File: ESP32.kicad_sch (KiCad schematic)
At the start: 5 parts

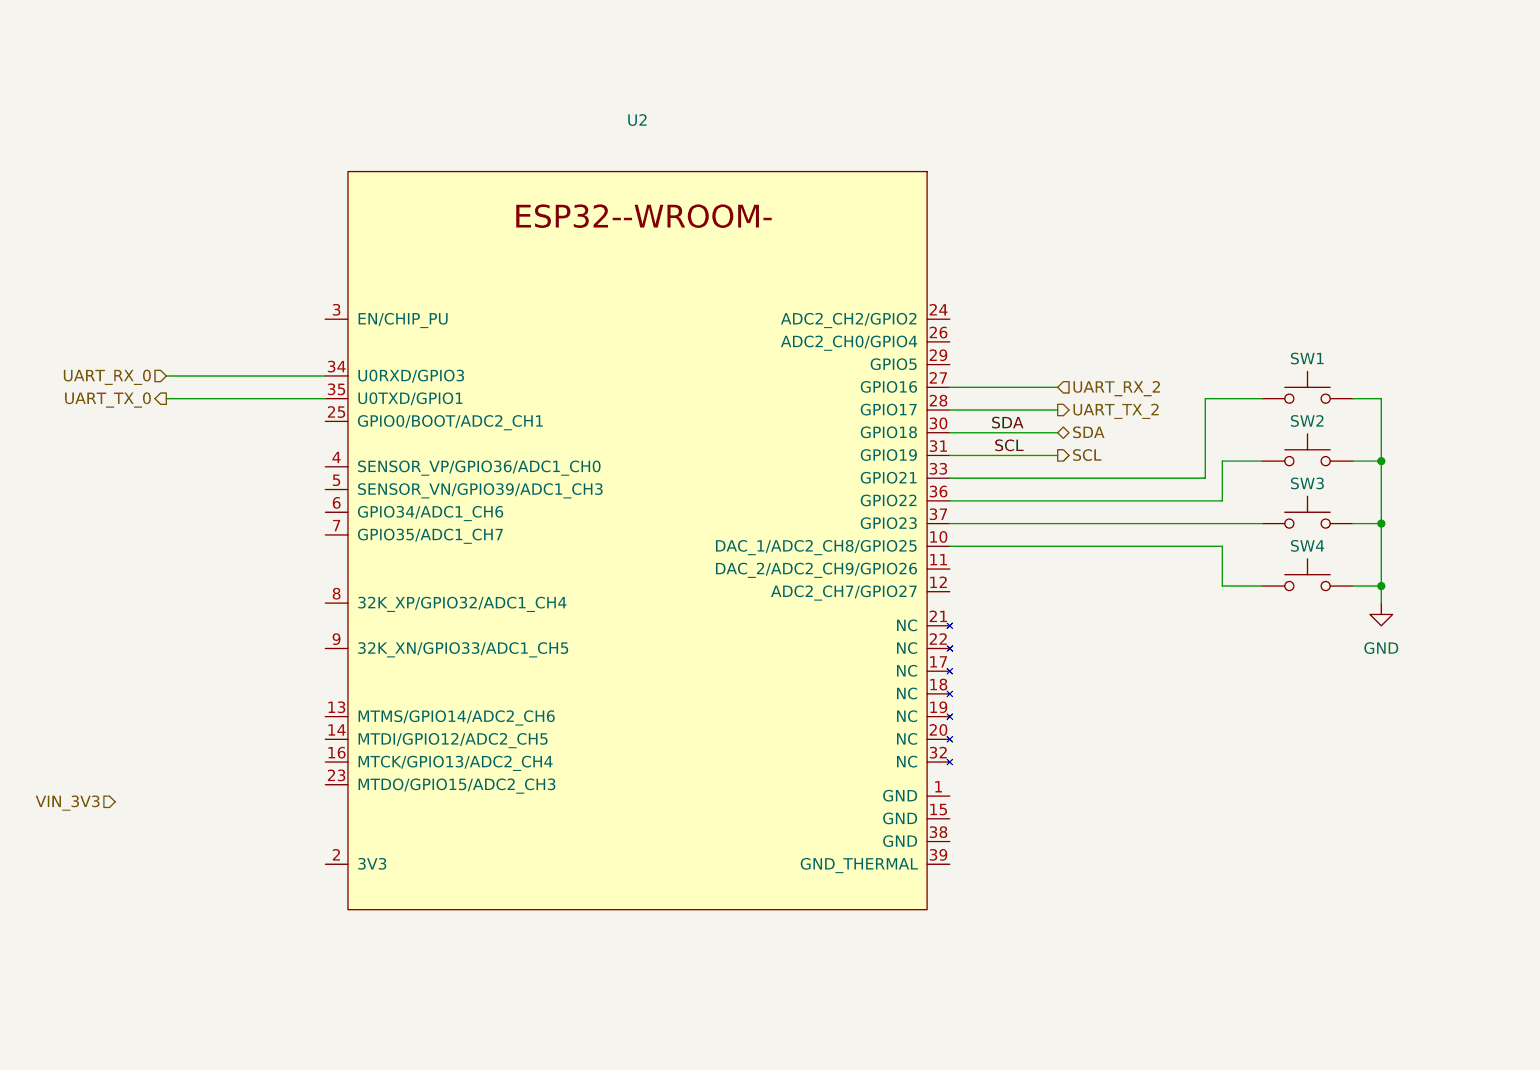
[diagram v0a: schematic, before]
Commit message: parcialmente terminada PCB falta verificar tamano de componentes
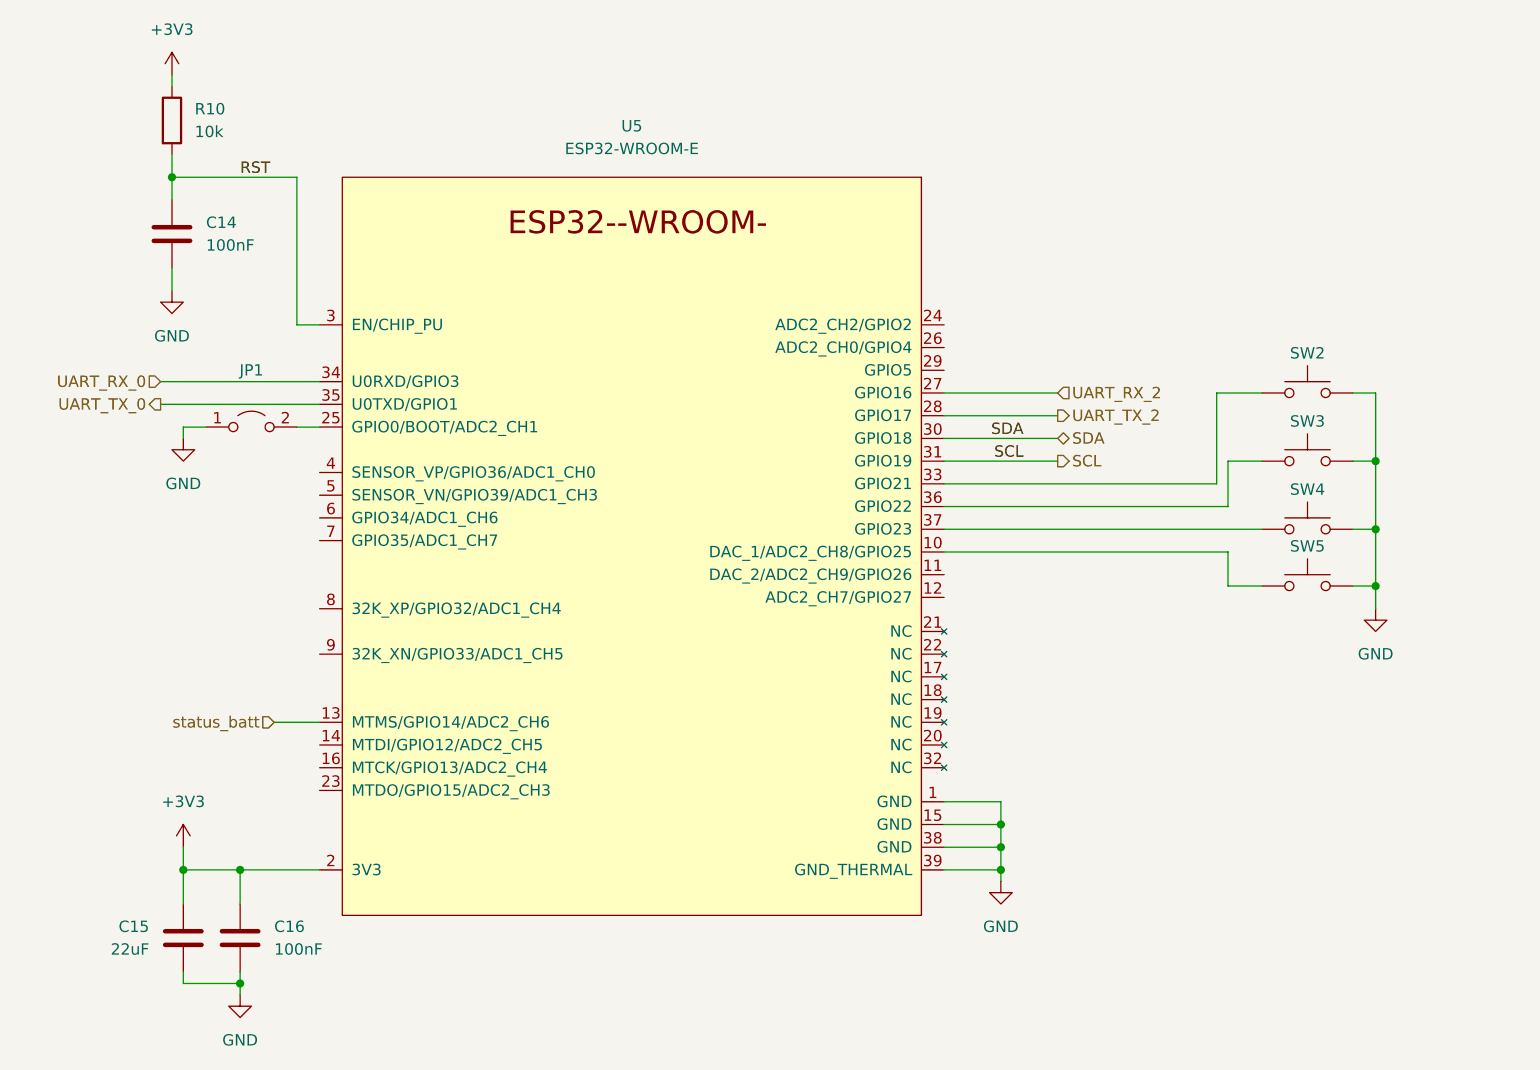
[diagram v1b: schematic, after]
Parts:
- added C14, C16: 100nF, Capacitor_SMD:C_0603_1608Metric_Pad1.08x0.95mm_HandSolder, symbol Device:C
- added C15: 22uF, Capacitor_SMD:C_0805_2012Metric_Pad1.18x1.45mm_HandSolder, symbol Device:C
- added JP1: (no value), symbol Jumper:Jumper_2_Open
- added R10: 10k, Resistor_SMD:R_0603_1608Metric_Pad0.98x0.95mm_HandSolder, symbol Device:R
- SW2: renamed from SW1; value (none) -> ~; footprint (none) -> Button_Switch_SMD:SW_SPST_PTS645
- SW3: renamed from SW2; value (none) -> ~; footprint (none) -> Button_Switch_SMD:SW_SPST_PTS645
- SW4: renamed from SW3; value (none) -> SW_Push; footprint (none) -> Button_Switch_SMD:SW_SPST_PTS645
- SW5: renamed from SW4; value (none) -> ~; footprint (none) -> Button_Switch_SMD:SW_SPST_PTS645
- U5: renamed from U2; value (none) -> ESP32-WROOM-E; footprint (none) -> Espressif:ESP32-WROOM-32E
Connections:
- net GND: now also U5.1 (GND), U5.15 (GND), U5.38 (GND), U5.39 (GND_THERMAL), C14.2, C15.2, C16.2, JP1.1 (A)
- net status_batt: now reaches U5.13 (MTMS/GPIO14/ADC2_CH6)
- net +3V3: now reaches U5.2 (3V3)
- net +3V3: now also C15.1, C16.1, R10.1
- net at U5.25 (GPIO0/BOOT/ADC2_CH1): now also JP1.2 (B)
- net RST: now reaches U5.3 (EN/CHIP_PU)
- net RST: now also C14.1, R10.2
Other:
- title: (none) -> GPS_CHECK
- moved on the sheet: SW2, SW4, U5

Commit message: terminando, aun falta una ultima revision previa a la fabricacion
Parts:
- JP1: value (none) -> Jumper_2_Open; footprint (none) -> Jumper:SolderJumper-2_P1.3mm_Open_RoundedPad1.0x1.5mm
- SW2, SW3, SW4, SW5: footprint Button_Switch_SMD:SW_SPST_PTS645 -> MSS_Devices:TL3301AF160QG
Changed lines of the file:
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@@
     (property "Reference" "SW5" (id 0) (at 222.25 98.425 0))
     (property "Value" "~" (id 1) (at 222.25 104.775 0))
-    (property "Footprint" "Button_Switch_SMD:SW_SPST_PTS645" (id 2) (at 222.25 97.79 0)
+    (property "Footprint" "MSS_Devices:TL3301AF160QG" (id 2) (at 222.25 97.79 0)
       (effects (font (size 1.27 1.27)) hide)
     )
@@
     (in_bom yes) (on_board yes) (fields_autoplaced)
     (property "Reference" "JP1" (id 0) (at 104.14 78.74 0))
-    (property "Value" "" (id 1) (at 104.14 81.28 0))
-    (property "Footprint" "" (id 2) (at 104.14 85.09 0)
+    (property "Value" "Jumper_2_Open" (id 1) (at 104.14 81.28 0))
+    (property "Footprint" "Jumper:SolderJumper-2_P1.3mm_Open_RoundedPad1.0x1.5mm" (id 2) (at 104.14 85.09 0)
       (effects (font (size 1.27 1.27)) hide)
     )
@@
     (property "Reference" "SW3" (id 0) (at 222.25 84.455 0))
     (property "Value" "~" (id 1) (at 222.25 83.185 0))
-    (property "Footprint" "Button_Switch_SMD:SW_SPST_PTS645" (id 2) (at 222.25 83.82 0)
+    (property "Footprint" "MSS_Devices:TL3301AF160QG" (id 2) (at 222.25 83.82 0)
       (effects (font (size 1.27 1.27)) hide)
     )
@@
       (effects (font (size 1.27 1.27)) hide)
     )
-    (property "Footprint" "Button_Switch_SMD:SW_SPST_PTS645" (id 2) (at 222.25 91.44 0)
+    (property "Footprint" "MSS_Devices:TL3301AF160QG" (id 2) (at 222.25 91.44 0)
       (effects (font (size 1.27 1.27)) hide)
     )
@@
     (property "Reference" "SW2" (id 0) (at 222.25 76.835 0))
     (property "Value" "~" (id 1) (at 222.25 75.565 0))
-    (property "Footprint" "Button_Switch_SMD:SW_SPST_PTS645" (id 2) (at 222.25 76.2 0)
+    (property "Footprint" "MSS_Devices:TL3301AF160QG" (id 2) (at 222.25 76.2 0)
       (effects (font (size 1.27 1.27)) hide)
     )

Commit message: generando gerbers
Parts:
- added R13, R14, R15, R16, R17, R18: 10k, Resistor_SMD:R_0603_1608Metric_Pad0.98x0.95mm_HandSolder, symbol Device:R
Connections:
- net +3V3: now also R15.1, R16.1, R17.1, R18.1
- net GND: now also R14.2
- net status_batt: now also R13.1; no longer U5.13 (MTMS/GPIO14/ADC2_CH6)
- net at SW5.1, U5.10 (DAC_1/ADC2_CH8/GPIO25): now also R18.2
- net at SW2.1, U5.33 (GPIO21): now also R15.2
- net at SW3.1, U5.36 (GPIO22): now also R16.2
- net at SW4.1, U5.37 (GPIO23): now also R17.2
- new net: R13.2, R14.1, U5.13 (MTMS/GPIO14/ADC2_CH6)
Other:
- moved on the sheet: SW2, SW3, SW4, SW5
